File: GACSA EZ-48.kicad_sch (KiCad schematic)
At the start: 7 parts, among them U1 6502, U2 6520, U3 6520, U4 SN76489, U5 TMS9918A

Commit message: Continuation on design
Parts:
- added E1, E2, E3, E4, E5, E6, E7, E8: 4116, symbol AppleII+:4116
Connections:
- net +5VDC: now also U2.22 (CS0), U2.24 (CS1), U3.22 (CS0), U3.24 (CS1), U5.33 (VCC), E1.9 (VCC), E2.9 (VCC), E3.9 (VCC), E4.9 (VCC), E5.9 (VCC), E6.9 (VCC), E7.9 (VCC), E8.9 (VCC)
- net GND: now also U5.12 (GND), E1.16 (GND), E2.16 (GND), E3.16 (GND), E4.16 (GND), E5.16 (GND), E6.16 (GND), E7.16 (GND), E8.16 (GND)
- net R/~{W}: now reaches U3.21 (R/~{W})
- net R/~{W}: now also U1.34 (R/~{W}), U2.21 (R/~{W})
- net ~{PIA0SEL}: now reaches U3.23 (~{CS2})
- net ~{RESET}: now reaches U3.34 (~{RESET})
- net ~{RESET}: now also U1.40 (~{RES}), U2.34 (~{RESET}), U5.34 (~{RESET})
- net A1: now reaches U3.35 (RS1)
- net A1: now also U1.10 (A1), U2.35 (RS1)
- net A0: now reaches U3.36 (RS0)
- net A0: now also U1.9 (A0), U2.36 (RS0), U5.13 (MODE)
- net PIA0CA1: now reaches U3.39 (CA2)
- net PIA0CA1: now also U3.40 (CA1)
- net A2: now reaches U1.11 (A2)
- net A3: now reaches U1.12 (A3)
- net A4: now reaches U1.13 (A4)
- net A5: now reaches U1.14 (A5)
- net A6: now reaches U1.15 (A6)
- net A7: now reaches U1.16 (A7)
- net A8: now reaches U1.17 (A8)
- net A9: now reaches U1.18 (A9)
- net A10: now reaches U1.19 (A10)
- net A11: now reaches U1.20 (A11)
- net A12: now reaches U1.22 (A12)
- net A13: now reaches U1.23 (A13)
- net A14: now reaches U1.24 (A14)
- net A15: now reaches U1.25 (A15)
- net PHI1: now reaches U1.3 (ϕ1)
- net PHI0: now reaches U1.37 (ϕ0)
- net PHI2: now reaches U1.39 (ϕ2)
- net ~{CPUIRQ}: now reaches U1.4 (~{IRQ})
- net ~{CPUNMI}: now reaches U1.6 (~{NMI})
- net ~{CPUNMI}: now also U5.16 (~{INT})
- net ~{VDPRAS}: now reaches U5.1 (~{RAS})
- net ~{VDPRAS}: now also E1.4 (~{RAS}), E2.4 (~{RAS}), E4.4 (~{RAS}), E5.4 (~{RAS}), E6.4 (~{RAS}), E7.4 (~{RAS}), E8.4 (~{RAS})
- net VRAM_ADDR: now reaches U5.10 (AD0)
- net VRAM_ADDR: now also U5.3 (AD7), U5.4 (AD6), U5.5 (AD5), U5.6 (AD4), U5.7 (AD3), U5.8 (AD2), U5.9 (AD1)
- net ~{VDPCSW}: now reaches U5.14 (~{CSW})
- net ~{VDPCSR}: now reaches U5.15 (~{CSR})
- net ~{VDPCAS}: now reaches U5.2 (~{CAS})
- net ~{VDPCAS}: now also E1.15 (~{CAS}), E2.15 (~{CAS}), E4.15 (~{CAS}), E5.15 (~{CAS}), E6.15 (~{CAS}), E7.15 (~{CAS}), E8.15 (~{CAS})
- net VRAM_DATA7: now reaches U5.25 (RD7)
- net VRAM_DATA6: now reaches U5.26 (RD6)
- net VRAM_DATA5: now reaches U5.27 (RD5)
- net VRAM_DATA4: now reaches U5.28 (RD4)
- net VRAM_DATA3: now reaches U5.29 (RD3)
- net VRAM_DATA2: now reaches U5.30 (RD2)
- net VRAM_DATA1: now reaches U5.31 (RD1)
- net VRAM_DATA0: now reaches U5.32 (RD0)
- net VIDEOIN: now reaches U5.35 (EXTVDP)
- net VIDOUT: now reaches U5.36 (COMVID)
- net 3.58MHz: now reaches U5.38 (CPUCLK)
- net ~{PIA1SEL}: now reaches U2.23 (~{CS2})
- net PIA1CA1: now reaches U2.39 (CA2)
- net PIA1CA1: now also U2.40 (CA1)
- new net +12VDC: E1.8 (VDD), E2.8 (VDD), E3.8 (VDD), E4.8 (VDD), E5.8 (VDD), E6.8 (VDD), E7.8 (VDD), E8.8 (VDD)
- new net -5VDC: E1.1 (VBB), E2.1 (VBB), E3.1 (VBB), E4.1 (VBB), E5.1 (VBB), E6.1 (VBB), E7.1 (VBB), E8.1 (VBB)
- no-connect marks 0 -> 2

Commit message: Advancing on the design
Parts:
- added C1, C2: 33pF, Capacitor_THT:C_Disc_D7.5mm_W5.0mm_P5.00mm, symbol Device:C
- added C3: 5-50pF, passives:C_Trimmer_THT_5mm, symbol Device:C_Trim_Small
- added X1: 10.7386MHz, Crystal:Crystal_HC49-U_Vertical, symbol Device:Crystal_GND3_Small
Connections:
- net GND: now also C1.1, C2.1, C3.1, X1.3
- net R/~{W}: now also U5.11 (R/~{W})
- net 1.79MHz: now reaches U4.14 (CLK)
- net PIA1CB1: now reaches R2.2, U2.18 (CB1), U4.5 (~{WE})
- net PIA1CB2: now reaches R1.2, U2.19 (CB2), U4.6 (~{CE})
- net PIA0CB1: now reaches U3.18 (CB1)
- net PIA0CB2: now reaches U3.19 (CB2)
- net VDPXTAL1: now reaches U5.39 (XTAL1)
- net VDPXTAL1: now also C1.2, X1.2
- net VDPXTAL2: now reaches U5.40 (XTAL2)
- net VDPXTAL2: now also C2.2, C3.2, X1.1

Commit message: Continued Development of VDP VRAM
Implemented VRAM Refresh
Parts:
- added C10, C13, C14: 10µF, Capacitor_THT:CP_Radial_D5.0mm_P2.00mm, symbol Device:C_Polarized_Small_US
- added C11, C12, C4, C5, C6, C7, C8, C9: 0.1µF, Capacitor_THT:C_Disc_D7.5mm_W2.5mm_P5.00mm, symbol Device:C
- added RA1: 1K, Resistor_THT:R_Array_SIP9, symbol Device:R_Network08_Split
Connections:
- net +5V: now also C14.1
- net +5VDC: now also RA1.1 (R1)
- net GND: now also U1.38 (~{SO}), C10.1, C11.2, C12.2, C13.2, C14.2, C4.1, C5.1, C6.1, C7.1, C8.2, C9.2
- net R/~{W}: no longer U5.11 (R/~{W})
- net VRAM_DATA0: now also E1.14 (D0), U5.25 (RD7); no longer U5.32 (RD0)
- net VRAM_DATA1: now also E2.14 (D0), U5.26 (RD6); no longer U5.31 (RD1)
- net VRAM_DATA2: now also E3.14 (D0), U5.27 (RD5); no longer U5.30 (RD2)
- net VRAM_DATA3: now also E4.14 (D0), U5.28 (RD4); no longer U5.29 (RD3)
- net VRAM_DATA4: now also E5.14 (D0), U5.29 (RD3); no longer U5.28 (RD4)
- net VRAM_DATA5: now also E6.14 (D0), U5.30 (RD2); no longer U5.27 (RD5)
- net VRAM_DATA6: now also E7.14 (D0), U5.31 (RD1); no longer U5.26 (RD6)
- net VRAM_DATA7: now also E8.14 (D0), U5.32 (RD0); no longer U5.25 (RD7)
- net ~{CPUIRQ}: now also U5.16 (~{INT})
- net ~{CPUNMI}: no longer U5.16 (~{INT})
- net ~{VDPCAS}: now also E3.15 (~{CAS})
- net ~{VDPRAS}: now also E3.4 (~{RAS})
- net VRAM_ADDR0: now reaches E3.10 (A0)
- net VRAM_ADDR0: now also E1.10 (A0), E1.2 (DI), E2.10 (A0), E4.10 (A0), E5.10 (A0), E6.10 (A0), E7.10 (A0), E8.10 (A0), U5.3 (AD7)
- net VRAM_ADDR1: now reaches E3.11 (A1)
- net VRAM_ADDR1: now also E1.11 (A1), E2.11 (A1), E2.2 (DI), E4.11 (A1), E5.11 (A1), E6.11 (A1), E7.11 (A1), E8.11 (A1), U5.4 (AD6)
- net VRAM_ADDR2: now reaches E3.12 (A2)
- net VRAM_ADDR2: now also E1.12 (A2), E2.12 (A2), E3.2 (DI), E4.12 (A2), E5.12 (A2), E6.12 (A2), E7.12 (A2), E8.12 (A2), U5.5 (AD5)
- net VRAM_ADDR6: now reaches E3.13 (A6)
- net VRAM_ADDR6: now also E1.13 (A6), E2.13 (A6), E4.13 (A6), E5.13 (A6), E6.13 (A6), E7.13 (A6), E7.2 (DI), E8.13 (A6), U5.9 (AD1)
- net VDPR/~{W}: now reaches E3.3 (R~{W})
- net VDPR/~{W}: now also E1.3 (R~{W}), E2.3 (R~{W}), E4.3 (R~{W}), E5.3 (R~{W}), E7.3 (R~{W}), E8.3 (R~{W}), U5.11 (R/~{W})
- net VRAM_ADDR5: now reaches E3.5 (A5)
- net VRAM_ADDR5: now also E1.5 (A5), E2.5 (A5), E4.5 (A5), E5.5 (A5), E6.2 (DI), E6.5 (A5), E7.5 (A5), E8.5 (A5), U5.8 (AD2)
- net VRAM_ADDR4: now reaches E3.6 (A4)
- net VRAM_ADDR4: now also E1.6 (A4), E2.6 (A4), E4.6 (A4), E5.2 (DI), E5.6 (A4), E6.6 (A4), E7.6 (A4), E8.6 (A4), U5.7 (AD3)
- net VRAM_ADDR3: now reaches E3.7 (A3)
- net VRAM_ADDR3: now also E1.7 (A3), E2.7 (A3), E4.2 (DI), E4.7 (A3), E5.7 (A3), E6.7 (A3), E7.7 (A3), E8.7 (A3), U5.6 (AD4)
- net at U1.2 (RDY): now also RA1.5 (R4.2)
- net VRAM_ADDR7: now reaches E8.2 (DI)
- net VRAM_ADDR7: now also U5.10 (AD0)
- removed net VRAM_ADDR: U5.10 (AD0), U5.3 (AD7), U5.4 (AD6), U5.5 (AD5), U5.6 (AD4), U5.7 (AD3), U5.8 (AD2), U5.9 (AD1)
- new net +12V: C11.1, C12.1, C13.1, C8.1, C9.1
- new net -5V: C10.2, C4.2, C5.2, C6.2, C7.2
- no-connect marks 2 -> 3
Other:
- note added: "VIDEO RAM"
- moved on the sheet: E1, E2, E3, E4, E5, E6, E7, E8

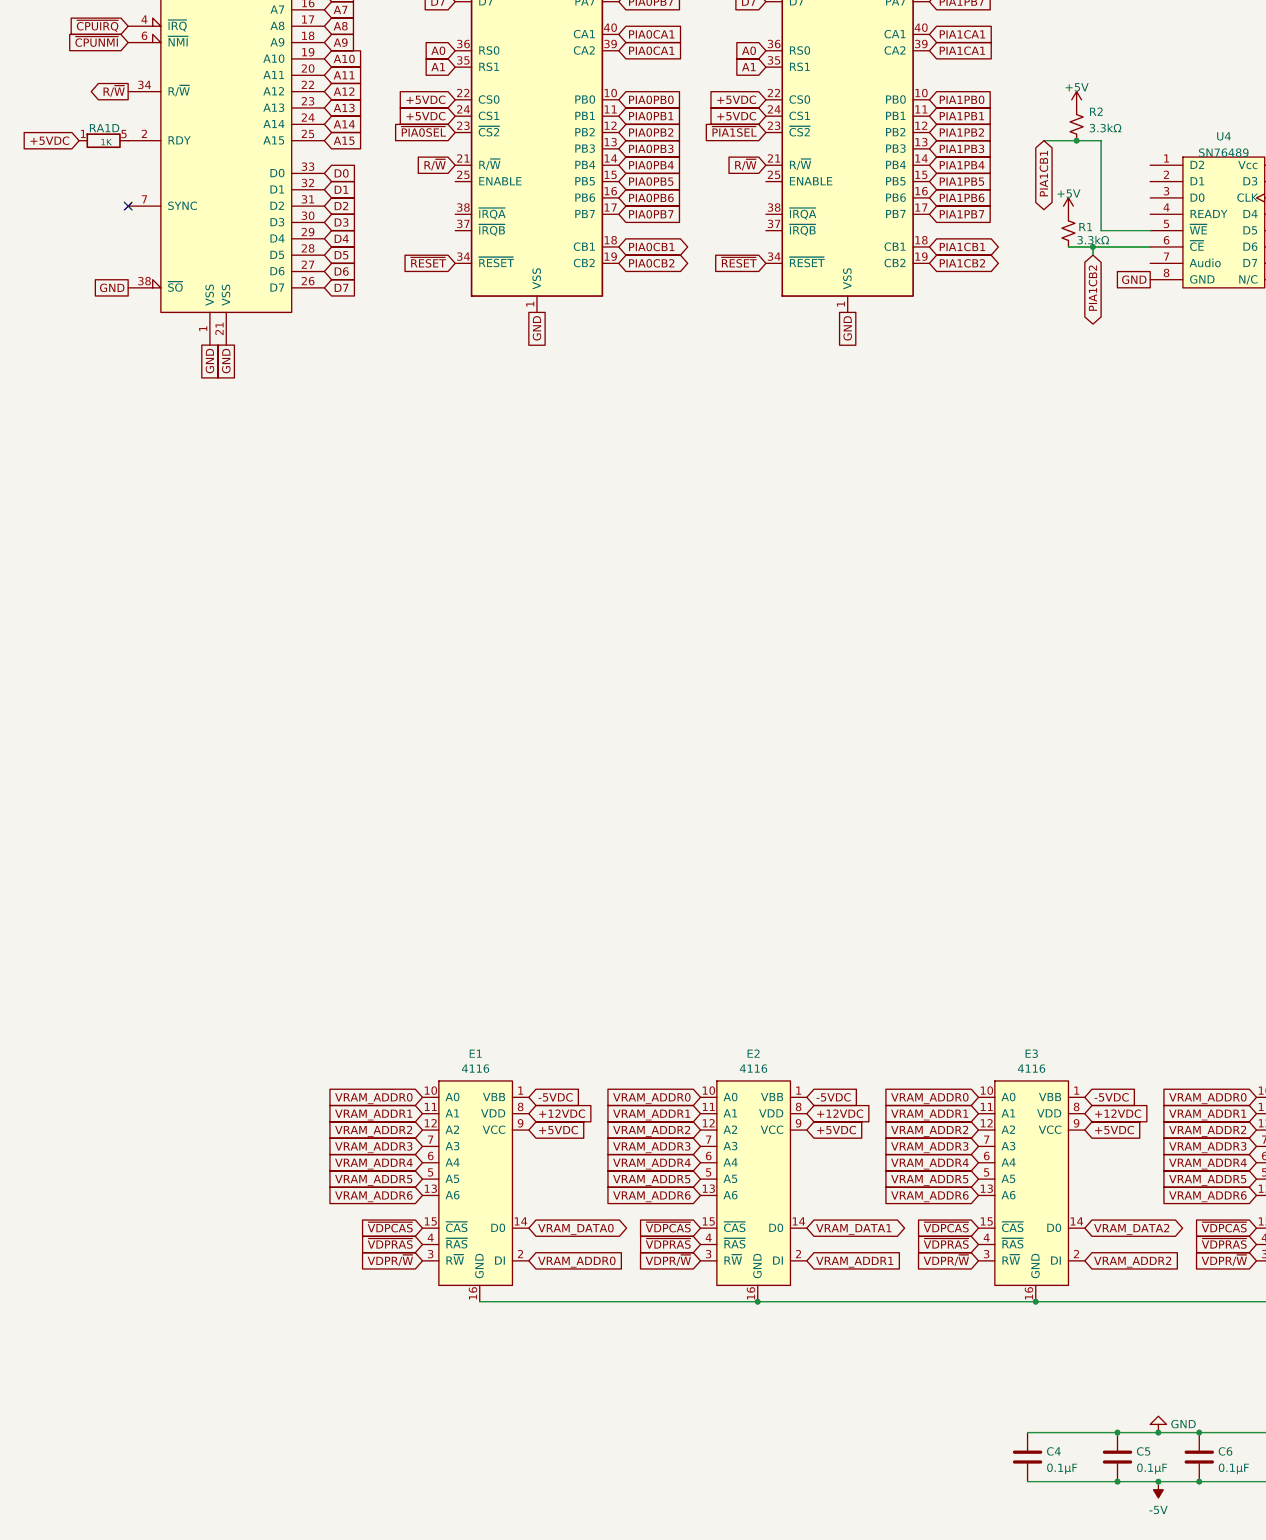
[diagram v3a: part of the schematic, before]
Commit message: Added keyboard connector
Added keyboard connector
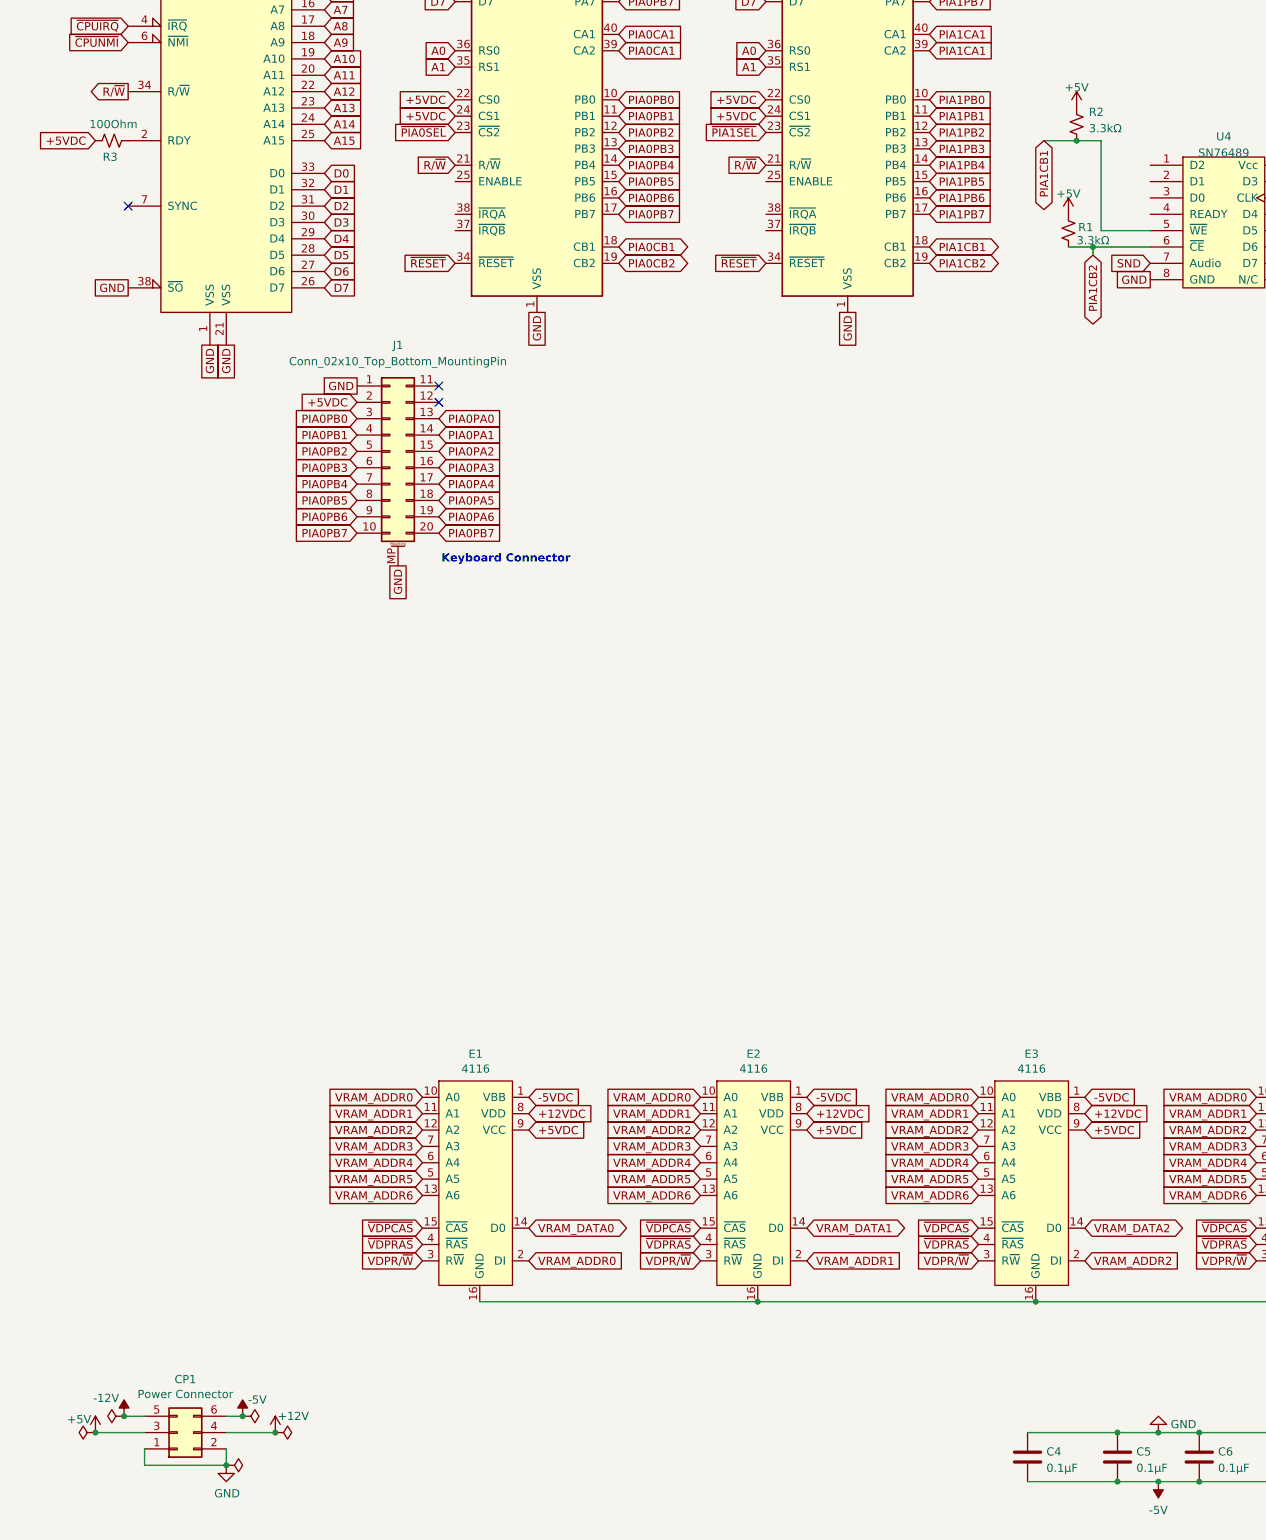
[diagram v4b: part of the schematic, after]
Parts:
- removed RA1: 1K, Resistor_THT:R_Array_SIP9, symbol Device:R_Network08_Split
- added CP1: Power Connector, Connector_IDC:IDC-Header_2x03_P2.54mm_Vertical, symbol Connector_Generic:Conn_02x03_Odd_Even
- added J1: Conn_02x10_Top_Bottom_MountingPin, Connector_IDC:IDC-Header_2x10-1MP_P2.54mm_Latch6.5mm_Vertical, symbol Connector_Generic_MountingPin:Conn_02x10_Top_Bottom_MountingPin
- added R3: 100Ohm, symbol Device:R_Small_US
- E1, E2, E3, E4, E5, E6, E7, E8: footprint (none) -> Package_DIP:DIP-16_W7.62mm_Socket_LongPads
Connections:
- net +12V: now also CP1.4 (Pin_4)
- net +5V: now also CP1.3 (Pin_3)
- net +5VDC: now also J1.2 (Pin_2), R3.1
- net -5V: now also CP1.6 (Pin_6)
- net GND: now also CP1.1 (Pin_1), CP1.2 (Pin_2), J1.1 (Pin_1), J1.MP (MountPin)
- net PIA0PA0: now also J1.13 (Pin_13)
- net PIA0PA1: now also J1.14 (Pin_14)
- net PIA0PA2: now also J1.15 (Pin_15)
- net PIA0PA3: now also J1.16 (Pin_16)
- net PIA0PA4: now also J1.17 (Pin_17)
- net PIA0PA5: now also J1.18 (Pin_18)
- net PIA0PA6: now also J1.19 (Pin_19)
- net PIA0PB0: now also J1.3 (Pin_3)
- net PIA0PB1: now also J1.4 (Pin_4)
- net PIA0PB2: now also J1.5 (Pin_5)
- net PIA0PB3: now also J1.6 (Pin_6)
- net PIA0PB4: now also J1.7 (Pin_7)
- net PIA0PB5: now also J1.8 (Pin_8)
- net PIA0PB6: now also J1.9 (Pin_9)
- net PIA0PB7: now also J1.10 (Pin_10), J1.20 (Pin_20)
- net at U1.2 (RDY): now also R3.2
- net SND: now reaches U4.7 (Audio)
- new net -12V: CP1.5 (Pin_5)
- no-connect marks 3 -> 5
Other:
- note added: "Keyboard Connector"

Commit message: Implemented Printer port and power connector
Implemented Printer port and power connector
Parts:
- added C15: 0.1uf, Capacitor_THT:C_Disc_D3.0mm_W1.6mm_P2.50mm, symbol Device:C
- added D17: LED, LED_THT:LED_D3.0mm, symbol Device:LED
- added J2: DIN-5_180degree, symbol Connector:DIN-5_180degree
- added J3, J4: Conn_01x10_Socket, Connector_PinSocket_2.54mm:PinSocket_1x10_P2.54mm_Vertical, symbol Connector:Conn_01x10_Socket
- added L1: Ferrite_Bead, Resistor_THT:R_Axial_DIN0207_L6.3mm_D2.5mm_P7.62mm_Horizontal, symbol Device:Ferrite_Bead
- added Q1: 2N4401, Package_TO_SOT_THT:TO-92L, symbol Device:Q_NPN_EBC
- added R4: 330Ω, Resistor_THT:R_Axial_DIN0207_L6.3mm_D2.5mm_P10.16mm_Horizontal, symbol Device:R_Small_US
- added R5: 75, Resistor_THT:R_Axial_DIN0207_L6.3mm_D2.5mm_P7.62mm_Horizontal, symbol Device:R
- added R6: R_Variable, Resistor_THT:R_Axial_DIN0207_L6.3mm_D2.5mm_P10.16mm_Horizontal, symbol Device:R_Variable
- added R7: 470, Resistor_THT:R_Axial_DIN0207_L6.3mm_D2.5mm_P7.62mm_Horizontal, symbol Device:R
- added U10, U9: 74LS244, Package_DIP:DIP-20_W7.62mm_LongPads, symbol 74xx:74LS244
- added U6: 74LS139, Package_DIP:DIP-16_W7.62mm_LongPads, symbol 74xx:74LS139
- added U7: 74LS74, symbol 74xx:74LS74
- added U8: 7400, symbol 74xx:7400
- X1: footprint Crystal:Crystal_HC49-U_Vertical -> Crystal:Crystal_HC49-4H_Vertical
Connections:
- net +12VDC: now also J2.1
- net +5V: now also D17.2 (A), J4.1 (Pin_1), J4.2 (Pin_2), L1.1, U7.1 (~{R}), U7.4 (~{S})
- net +5VDC: now also U6.16 (VCC)
- net 3.58MHz: now also U7.3 (C)
- net A12: now also U6.14 (A0)
- net A13: now also U6.13 (A1)
- net A14: now also U6.2 (A0)
- net A15: now also U6.3 (A1)
- net GND: now also C15.2, J2.2, R4.2, R5.2, R7.2, U6.1 (E), U6.8 (GND), U9.1 (OEa), U9.10 (GND), U9.19 (OEb)
- net PHI2: now also U8.1, U8.5
- net PIA1CB1: now also U4.4 (READY)
- net PIA1PA0: now also U9.2 (I0a)
- net PIA1PA1: now also U9.4 (I1a)
- net PIA1PA2: now also U9.6 (I2a)
- net PIA1PA3: now also U9.8 (I3a)
- net PIA1PA4: now also U9.11 (I0b)
- net PIA1PA5: now also U9.13 (I1b)
- net PIA1PA6: now also U9.15 (I2b)
- net PIA1PB0: now also U4.10 (D7)
- net PIA1PB1: now also U4.11 (D6)
- net PIA1PB2: now also U4.12 (D5)
- net PIA1PB3: now also U4.13 (D4)
- net PIA1PB4: now also U4.15 (D3)
- net PIA1PB5: now also U4.1 (D2)
- net PIA1PB6: now also U4.2 (D1)
- net PIA1PB7: now also U4.3 (D0), U9.17 (I3b)
- net R/~{W}: now also U8.10, U8.2, U8.9
- net VIDOUT: now also J2.4, Q1.1 (E), R5.1, R6.1
- net PHI0 renamed 1.79Mhz
- net 1.79Mhz: now also U7.5 (Q)
- net SND renamed PSGSND
- new net: Q1.2 (B), R6.2, R7.1
- new net: C15.1, L1.2, Q1.3 (C)
- new net: J3.4 (Pin_4), U9.12 (O3a)
- new net: J3.3 (Pin_3), U9.14 (O2a)
- new net: J3.2 (Pin_2), U9.16 (O1a)
- new net: J3.1 (Pin_1), U9.18 (O0a)
- new net: J3.8 (Pin_8), U9.3 (O3b)
- new net: J3.7 (Pin_7), U9.5 (O2b)
- new net: J3.6 (Pin_6), U9.7 (O1b)
- new net: J3.5 (Pin_5), U9.9 (O0b)
- new net: D17.1 (K), R4.1
- new net: U8.4, U8.8
- new net: J4.3 (Pin_3), J4.4 (Pin_4), J4.5 (Pin_5), J4.6 (Pin_6), J4.7 (Pin_7), J4.8 (Pin_8), J4.9 (Pin_9)
- new net: U7.2 (D), U7.6 (~{Q})
- new net ACK: J3.9 (Pin_9)
- new net BUSY: J4.10 (Pin_10)
- new net SOUNDOUT: J2.3, J2.5
- new net ~{C000-CFFF}: U6.12 (O0)
- new net ~{C000-FFFF}: U6.15 (E), U6.7 (O3)
- new net ~{RAM0}: U6.4 (O0)
- new net ~{RAM1}: U6.5 (O1)
- new net ~{RAM2}: U6.6 (O2)
- new net ~{READ}: U8.3
- new net ~{ROM0}: U6.11 (O1)
- new net ~{ROM1}: U6.10 (O2)
- new net ~{ROM2}: U6.9 (O3)
- new net ~{WRITE}: U8.6
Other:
- note added: "0-200Ohm"
- note added: "PARALLEL PORT"
- note added: "READ/WRITE LOGIC"
- moved on the sheet: C10, C11, C12, C13, C14, C4, C5, C6, C7, C8, C9, CP1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
